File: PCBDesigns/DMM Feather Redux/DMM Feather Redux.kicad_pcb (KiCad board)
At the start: 4 copper layers, 116.2 x 93.3 mm, 49 parts, among them J10 I_Input, J14 Barrel_Jack, J2 Conn_01x03_Pin, J3 Conn_01x04_MountingPin, J7 Barrel_Jack, Q2 AO3400A MOSFET, Q8 AO3400A MOSFET, SW3 SW_SPDT, U10 LM4040DBZ-2.5, U13 ISO1540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

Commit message: Work on different PCBs. Mostly.
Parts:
- removed A1: Adafruit_Feather_32u4_BluefruitLE, Module:Adafruit_Feather_WithMountingHoles
- removed H1, H2, H3: MountingHole, MountingHole:MountingHole_2.2mm_M2_Pad
- removed H4: MountingHole, MountingHole:MountingHole_2.2mm_M2_ISO14580
- removed J2: Conn_01x03_Pin, Connector_PinHeader_2.54mm:PinHeader_1x03_P2.54mm_Vertical
- removed R6, R7: 4.7K, Resistor_SMD:R_0805_2012Metric_Pad1.20x1.40mm_HandSolder
- added A2: Adafruit_Feather_32u4_BluefruitLE, Module:Adafruit_Feather_WithMountingHoles, F.Cu at (47.9, 64.3)
- added D1: LED, LED_SMD:LED_Luminus_MP-3030-1100_3.0x3.0mm, F.Cu at (143.5, 80.2)
- added J5: Conn_01x12_Pin, Connector_PinSocket_2.54mm:PinSocket_1x12_P2.54mm_Vertical, F.Cu at (126.2, 93.2)
- added J6: Conn_01x16_Pin, Connector_PinSocket_2.54mm:PinSocket_1x16_P2.54mm_Vertical, F.Cu at (116.1, 113.5)
- added J9: Out to Screen, Connector_PinSocket_2.54mm:PinSocket_1x04_P2.54mm_Vertical, F.Cu at (221.4, 71.1)
- added Q1: MMBT3904, Package_TO_SOT_SMD:SOT-23, F.Cu at (148.3, 80.2)
- added R4: 500, Resistor_SMD:R_0805_2012Metric_Pad1.20x1.40mm_HandSolder, F.Cu at (154.9, 80.2)
- added RN1: R_Pack04_Split, Resistor_SMD:R_Array_Convex_4x0603, F.Cu at (158.1, 98.0)
- added SW1: SW_Push, Button_Switch_SMD:SW_SPST_CK_RS282G05A3, F.Cu at (131.3, 76.6)
- added SW2: SW_Push, Button_Switch_SMD:SW_SPST_CK_RS282G05A3, F.Cu at (131.3, 81.8)
- added SW4: SW_Push, Button_Switch_SMD:SW_SPST_CK_RS282G05A3, F.Cu at (131.3, 86.9)
- C17, C4, C7, C8: footprint Capacitor_SMD:C_0805_2012Metric_Pad1.18x1.45mm_HandSolder -> Capacitor_SMD:C_0603_1608Metric
- R1, R10, R11, R12, R19, R2, R27: footprint Resistor_SMD:R_0805_2012Metric_Pad1.20x1.40mm_HandSolder -> Resistor_SMD:R_0603_1608Metric
- R5: value 4.7K -> 1K; footprint Resistor_SMD:R_0805_2012Metric_Pad1.20x1.40mm_HandSolder -> Resistor_SMD:R_0603_1608Metric
- moved U4 60.5 mm to (135.9, 103.3), turned to 90 degrees
- moved J7 52.0 mm to (183.4, 89.9), turned to 180 degrees
- moved J3 33.6 mm to (117.2, 93.7)
- moved C7 32.0 mm to (145.5, 108.0), turned to 180 degrees
- moved R10 32.0 mm to (175.4, 114.4), turned to 180 degrees
- moved C6 31.2 mm to (165.5, 82.0), turned to 90 degrees
- moved J10 30.0 mm to (187.5, 74.0)
- moved U6 30.0 mm to (168.6, 82.0), turned to 90 degrees
- moved R2 28.9 mm to (151.2, 98.4), turned to 180 degrees
- moved R12 28.4 mm to (157.7, 108.8)
- moved Q8 27.8 mm to (171.8, 111.8), turned to 90 degrees
- moved J14 26.7 mm to (183.5, 106.2), turned to 180 degrees
- moved R17 25.6 mm to (176.9, 109.3), turned to 180 degrees
- moved U13 25.3 mm to (145.4, 103.1), turned to -90 degrees
- moved SW3 24.6 mm to (118.8, 78.6), turned to -90 degrees
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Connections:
- net /MOSFET_Gate renamed /V_Bridge_Ctrl-ISO
- R5 pad 1: 5V-iso -> /LED_Ctrl_ISO
- R5 pad 2: SCL-5V -> Net-(Q1-B)
- U4 pad 11: unconnected-(U4-VOD-Pad11) -> /LED_Ctrl_ISO
- U4 pad 6: unconnected-(U4-VID-Pad6) -> /LED_Ctrl
- U5 pad 3: /Driver_U2_Out_B -> /I_Supply_Ohmmeter
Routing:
- net SCL: track 48.3 -> 0.00 mm, vias 1 -> 0
- net SDA: track 44.6 -> 0.00 mm, vias 3 -> 0
- net /R Circuit I Output: track 0.00 -> 25.7 mm
- net VDD: track 21.9 -> 0.00 mm, vias 1 -> 0
- net SDA-5V: track 24.5 -> 3.34 mm, vias 2 -> 0
- net 5V-iso: track 22.0 -> 3.75 mm, vias 7 -> 2
- net /V_Bridge_Ctrl-ISO: track 31.9 -> 14.6 mm
- net Net-(Q2-S): track 0.00 -> 17.2 mm
- net SCL-5V: track 20.2 -> 3.38 mm, vias 2 -> 0
- net GND: track 15.2 -> 0.00 mm
- net Net-(Q2-G): track 0.00 -> 15.0 mm, vias 0 -> 2
- net Gnd-iso: track 28.0 -> 15.9 mm, vias 6 -> 8
- net ADS_ALERT: track 11.8 -> 0.00 mm
- net Net-(U5-VO): track 0.00 -> 9.45 mm
- net ADS_ADDR: track 8.07 -> 0.00 mm
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- removed copper zone on In1.Cu, net GND
- removed copper zone on In2.Cu, net VDD
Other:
- board size 116.2 x 93.3 mm -> 80.9 x 47.9 mm

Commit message: More PCB work.
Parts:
- moved A2 84.1 mm to (116.1, 113.5)
- moved J9 41.2 mm to (180.2, 72.4)
- moved R19 14.5 mm to (168.5, 94.2)
- moved SW1 10.2 mm to (131.3, 86.9)
- moved SW4 9.21 mm to (131.3, 77.7)
- moved R4 6.99 mm to (148.0, 80.0)
- moved J3 6.53 mm to (119.5, 87.6)
- moved R12 6.41 mm to (164.1, 108.8)
- moved C4 6.33 mm to (161.2, 103.6)
- moved U3 6.33 mm to (164.3, 103.6)
- moved U10 6.21 mm to (169.4, 101.2)
- moved J10 4.85 mm to (192.3, 74.9)
- moved Q1 4.78 mm to (148.0, 75.5)
- moved D1 4.56 mm to (143.9, 75.6), turned to 90 degrees
- moved SW3 4.06 mm to (120.2, 74.8)
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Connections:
- net Net-(A2-EN) renamed EN
- A2 pad 10: unconnected-(A2-A5-Pad10) -> A5
- A2 pad 11: unconnected-(A2-SCK/D15-Pad11) -> SCK
- A2 pad 12: unconnected-(A2-MOSI/D16-Pad12) -> MOSI
- A2 pad 13: unconnected-(A2-MISO/D14-Pad13) -> MISO
- A2 pad 14: unconnected-(A2-RX/D0-Pad14) -> RX
- A2 pad 15: unconnected-(A2-TX/D1-Pad15) -> TX
- A2 pad 19: /V_Bridge_Ctrl-MCU -> D5
- A2 pad 20: /LED_Ctrl -> D6
- A2 pad 21: /D9_(OhmmeterBridge_ctrl) -> D9
- A2 pad 22: /D10_(Ohmmeter_I_ctrl) -> D10
- A2 pad 26: unconnected-(A2-USB-Pad26) -> USB
- A2 pad 28: unconnected-(A2-VBAT-Pad28) -> VBAT
- A2 pad 5: unconnected-(A2-A0-Pad5) -> A0
- A2 pad 6: unconnected-(A2-A1-Pad6) -> A1
- A2 pad 7: unconnected-(A2-A2-Pad7) -> A2
- A2 pad 8: unconnected-(A2-A3-Pad8) -> A3
- A2 pad 9: unconnected-(A2-A4-Pad9) -> A4
- D1 pad 1: GND -> Gnd-iso
- J5 pad 1: unconnected-(J5-Pin_1-Pad1) -> VBAT
- J5 pad 10: /V_Bridge_Ctrl-MCU -> D5
- J5 pad 3: unconnected-(J5-Pin_3-Pad3) -> USB
- J5 pad 4: unconnected-(J5-Pin_4-Pad4) -> D13
- J5 pad 5: unconnected-(J5-Pin_5-Pad5) -> D12
- J5 pad 6: unconnected-(J5-Pin_6-Pad6) -> D11
- J5 pad 7: /D10_(Ohmmeter_I_ctrl) -> D10
- J5 pad 8: /D9_(OhmmeterBridge_ctrl) -> D9
- J5 pad 9: unconnected-(J5-Pin_9-Pad9) -> D6
- J6 pad 1: unconnected-(J6-Pin_1-Pad1) -> RESET
- J6 pad 10: unconnected-(J6-Pin_10-Pad10) -> A5
- J6 pad 11: unconnected-(J6-Pin_11-Pad11) -> SCK
- J6 pad 12: unconnected-(J6-Pin_12-Pad12) -> MOSI
- J6 pad 13: unconnected-(J6-Pin_13-Pad13) -> MISO
- J6 pad 14: unconnected-(J6-Pin_14-Pad14) -> RX
- J6 pad 15: unconnected-(J6-Pin_15-Pad15) -> TX
- J6 pad 3: unconnected-(J6-Pin_3-Pad3) -> VDD
- J6 pad 5: unconnected-(J6-Pin_5-Pad5) -> A0
- J6 pad 6: unconnected-(J6-Pin_6-Pad6) -> A1
- J6 pad 7: unconnected-(J6-Pin_7-Pad7) -> A2
- J6 pad 8: unconnected-(J6-Pin_8-Pad8) -> A3
- J6 pad 9: unconnected-(J6-Pin_9-Pad9) -> A4
- J9 pad 1: SDA-5V -> SDA
- J9 pad 2: SCL-5V -> SCL
- RN1 pad 2: unconnected-(RN1B-R2.1-Pad2) -> 5V-iso
- U4 pad 3: /D9_(OhmmeterBridge_ctrl) -> D5
- U4 pad 4: /D10_(Ohmmeter_I_ctrl) -> D6
- U4 pad 5: /V_Bridge_Ctrl-MCU -> D9
- U4 pad 6: /LED_Ctrl -> D10
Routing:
- net /AIN3: track 0.00 -> 36.2 mm, vias 0 -> 2
- net Gnd-iso: track 15.9 -> 49.6 mm, vias 8 -> 14
- net D11: track 0.00 -> 20.3 mm
- net D5: track 0.00 -> 16.1 mm
- net SDA-5V: track 3.34 -> 18.7 mm
- net SCL-5V: track 3.38 -> 18.7 mm, vias 0 -> 2
- net D6: track 0.00 -> 15.0 mm
- net D12: track 0.00 -> 14.8 mm
- net D9: track 0.00 -> 13.7 mm
- net Net-(Q2-S): track 17.2 -> 30.0 mm
- net SDA: track 0.00 -> 12.7 mm, vias 0 -> 2
- net D10: track 0.00 -> 12.5 mm
- net SCL: track 0.00 -> 11.9 mm, vias 0 -> 2
- net 5V-iso: track 3.75 -> 15.5 mm, vias 2 -> 6
- net ADS_ALERT: track 0.00 -> 11.2 mm, vias 0 -> 2
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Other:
- board size 80.9 x 47.9 mm -> 83.4 x 47.9 mm

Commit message: PCB Work.
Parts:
- removed A2: Adafruit_Feather_32u4_BluefruitLE, Module:Adafruit_Feather_WithMountingHoles
- removed J3: Conn_01x04_MountingPin, Connector_JST:JST_SH_SM04B-SRSS-TB_1x04-1MP_P1.00mm_Horizontal
- removed SW3: SW_SPDT, Button_Switch_THT:SW_Slide_SPDT_Angled_CK_OS102011MA1Q
- added C10: 0.1uF, Capacitor_SMD:C_0603_1608Metric, F.Cu at (140.6, 97.8)
- added C11: 0.1uF, Capacitor_SMD:C_0603_1608Metric, F.Cu at (137.9, 110.5)
- added SW5: MS-22D28-G020, Library:SW-SMD_MS-22D28-G020, F.Cu at (119.4, 81.9)
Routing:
- net GND: track 3.09 -> 52.7 mm, vias 0 -> 7
- net Gnd-iso: track 49.6 -> 96.3 mm, vias 14 -> 17
- net VDD: track 3.18 -> 45.1 mm, vias 0 -> 3
- net /V_Bridge_Ctrl-ISO: track 5.41 -> 46.2 mm, vias 0 -> 2
- net 5V-iso: track 15.5 -> 54.7 mm, vias 6 -> 7
- net /LED_Ctrl_ISO: track 0.00 -> 36.9 mm, vias 0 -> 2
- net /OhmmeterBridgeCtrl_ISO: track 0.00 -> 36.4 mm, vias 0 -> 2
- net /Ohmmeter_I_ctrl_ISO: track 0.00 -> 35.3 mm, vias 0 -> 2
- net SDA: track 12.7 -> 47.4 mm
- net SCL: track 11.9 -> 46.6 mm
- net EN: track 0.00 -> 17.4 mm
- net Net-(J10-Pin_2): track 2.99 -> 8.14 mm
- net ADS_ALERT: track 11.2 -> 14.8 mm
- net SDA-5V: track 18.7 -> 22.3 mm, vias 0 -> 2
- net SCL-5V: track 18.7 -> 22.0 mm
- added copper zone on In1.Cu, net GND
- added copper zone on In2.Cu, net VDD
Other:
- board size 83.4 x 47.9 mm -> 85.5 x 47.4 mm

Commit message: PCB Work
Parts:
- SW1, SW2, SW4: footprint Button_Switch_SMD:SW_SPST_CK_RS282G05A3 -> Button_Switch_SMD:SW_Push_1P1T-SH_NO_CK_KMR2xxG
- moved SW2 40.0 mm to (94.9, 98.7)
- moved SW4 34.4 mm to (100.1, 92.3)
- moved SW1 31.4 mm to (104.3, 102.7)
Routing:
- net Gnd-iso: track 96.3 -> 92.8 mm, vias 17 -> 16
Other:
- board text added: "OIH Designs Feather-Based DMM 20260529"
- board text removed: "OIH Designs | Voltmeter Above Ground Bias w Open Lead Detect Vout = (+Vin/((R17+18)/R24))-VRef) Input safe voltages only w/o extra precautions & testing."

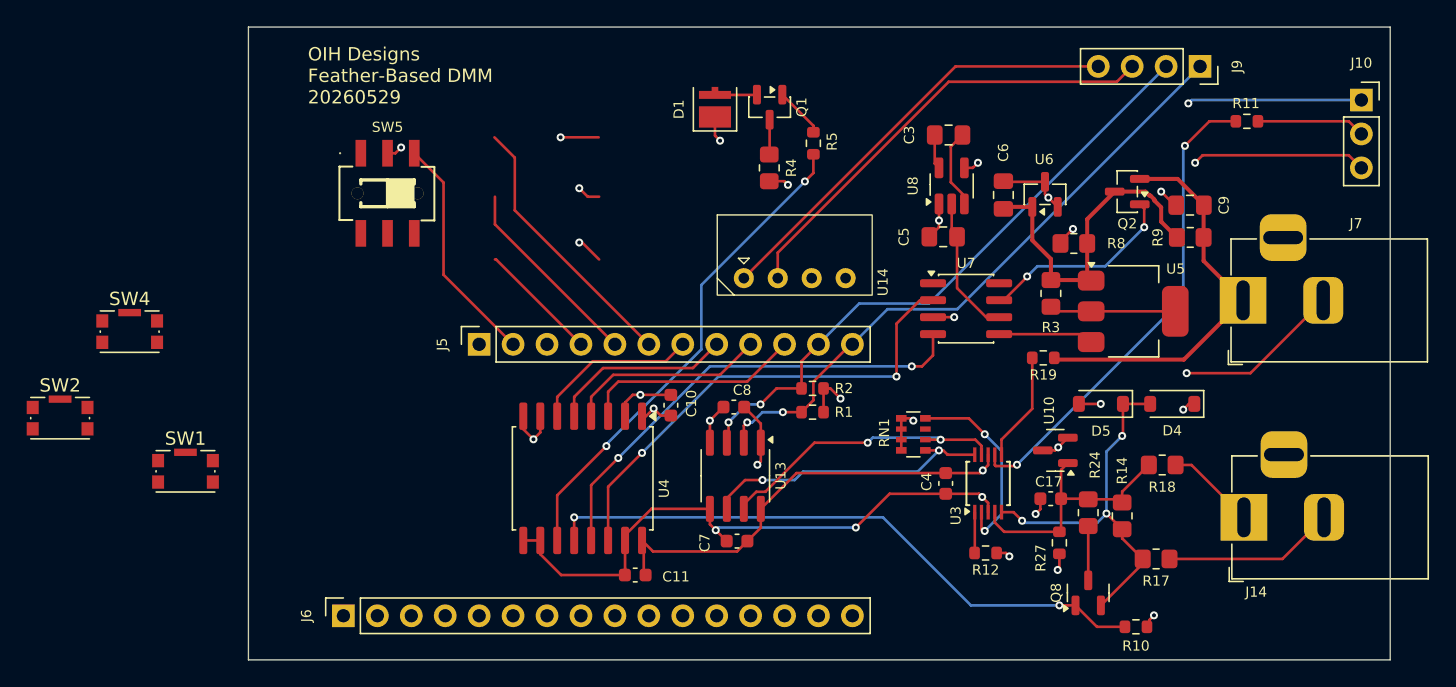
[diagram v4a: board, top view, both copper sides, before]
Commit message: DMM PCB work and Voltmeter Sketch Updates
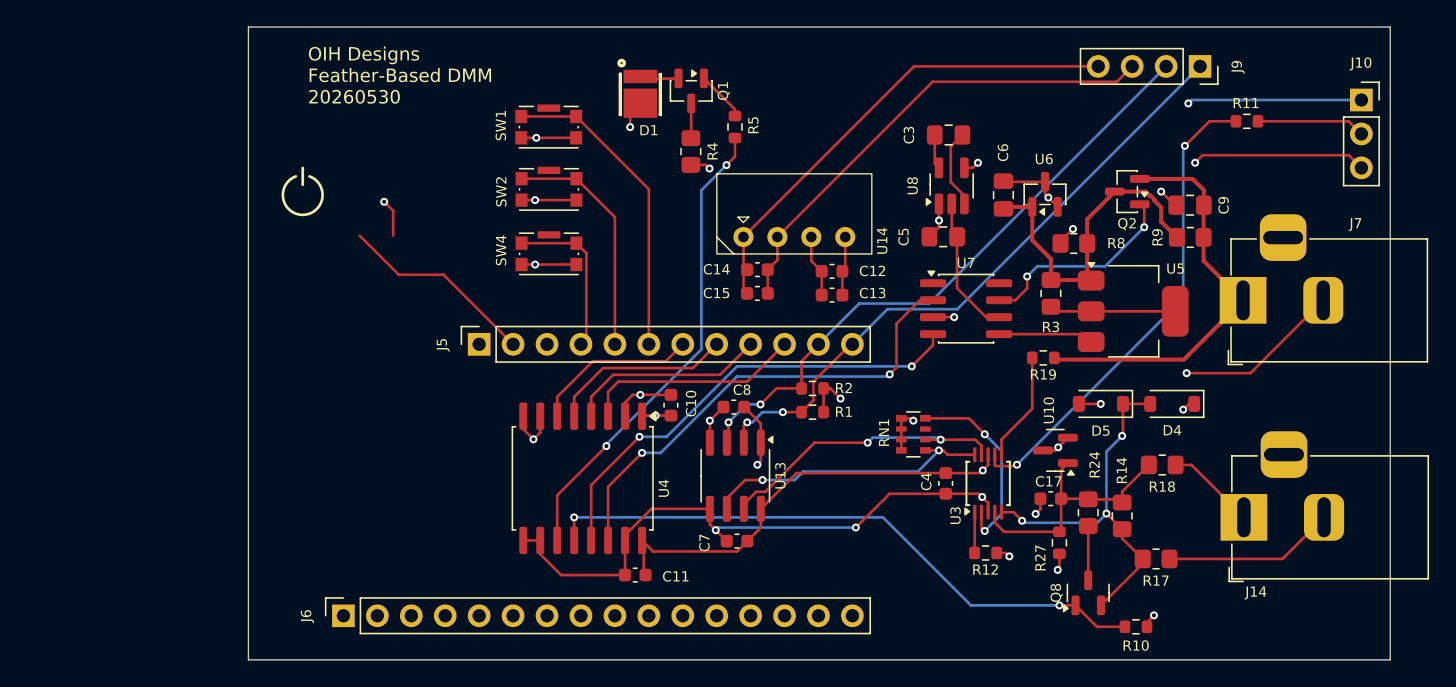
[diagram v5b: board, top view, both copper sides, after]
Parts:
- removed SW5: MS-22D28-G020, Library:SW-SMD_MS-22D28-G020
- added C12: 10uF, Capacitor_SMD:C_0603_1608Metric, F.Cu at (152.7, 87.8)
- added C13: 0.1uF, Capacitor_SMD:C_0603_1608Metric, F.Cu at (152.7, 89.5)
- added C14: 10uF, Capacitor_SMD:C_0603_1608Metric, F.Cu at (147.1, 87.6)
- added C15: 0.1uF, Capacitor_SMD:C_0603_1608Metric, F.Cu at (147.1, 89.4)
- D1: footprint LED_SMD:LED_Luminus_MP-3030-1100_3.0x3.0mm -> Custom:LED-SMD_L3.0-W3.0_WHITE
- moved SW2 40.4 mm to (131.5, 81.6)
- moved SW1 37.5 mm to (131.4, 77.0)
- moved SW4 31.9 mm to (131.5, 86.4)
- moved Q1 5.99 mm to (142.1, 74.2)
- moved R4 5.99 mm to (142.1, 78.8)
- moved R5 5.99 mm to (145.4, 76.9)
- moved D1 5.77 mm to (138.3, 74.2), turned to -90 degrees
- moved U14 3.08 mm to (151.1, 84.1)
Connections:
- D1 pad 1: Gnd-iso -> Net-(D1-A)
- D1 pad 2: Net-(D1-A) -> Gnd-iso
- SW1 pad 1: D13 -> D11
- SW4 pad 1: D11 -> D13
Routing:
- net GND: track 52.7 -> 63.1 mm
- net 5V-iso: track 54.7 -> 59.1 mm
- net Gnd-iso: track 92.8 -> 96.6 mm
- net D11: track 20.3 -> 23.4 mm
- net D13: track 9.07 -> 12.1 mm
- net D12: track 14.8 -> 17.7 mm
- net EN: track 17.4 -> 14.8 mm
- net VDD: track 45.1 -> 46.9 mm
- net /LED_Ctrl_ISO: track 36.9 -> 35.6 mm
- net Net-(Q2-S): track 30.0 -> 30.6 mm
- net Net-(Q2-G): track 15.0 -> 15.5 mm
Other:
- board text added: "OIH Designs Feather-Based DMM 20260530"
- board text removed: "OIH Designs Feather-Based DMM 20260529"

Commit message: Circuits, mostly
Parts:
- added A2: Adafruit_Feather_32u4_BluefruitLE, Module:Adafruit_Feather_WithMountingHoles, F.Cu at (1.76, 6.62)
- added J1: Conn_01x02, Connector_PinSocket_2.54mm:PinSocket_1x02_P2.54mm_Vertical, F.Cu at (116.7, 83.3)
- added J2: Conn_01x02, Connector_PinSocket_2.54mm:PinSocket_1x02_P2.54mm_Vertical, F.Cu at (124.3, 102.1)
- added R20: 240k, Resistor_SMD:R_0805_2012Metric, F.Cu at (179.2, 103.4)
- added R21: 240k, Resistor_SMD:R_0805_2012Metric, F.Cu at (178.0, 111.8)
- R14, R24, R3, R4, R8, R9: footprint Resistor_SMD:R_0805_2012Metric_Pad1.20x1.40mm_HandSolder -> Resistor_SMD:R_0805_2012Metric
- R17, R18: value 499.0K -> 240k; footprint Resistor_SMD:R_0805_2012Metric_Pad1.20x1.40mm_HandSolder -> Resistor_SMD:R_0805_2012Metric
- moved D5 19.0 mm to (160.4, 112.1)
- moved D4 19.0 mm to (165.7, 112.1)
- moved R10 17.9 mm to (159.5, 106.2)
- moved R18 2.24 mm to (175.1, 102.2)
- moved R17 0.76 mm to (176.1, 109.3)
- moved SW1 0.25 mm to (131.4, 76.7)
- renumbered SW4 to SW3
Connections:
- R17 pad 1: V_Input_Float -> Net-(R17-Pad1)
- R18 pad 1: V_Input_REF -> Net-(R18-Pad1)
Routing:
- net VBAT: track 0.00 -> 9.68 mm
- net Net-(R18-Pad1): track 0.00 -> 3.25 mm
- net GND: track 63.1 -> 60.3 mm, vias 7 -> 6
- net /V_Bridge_Ctrl-ISO: track 46.2 -> 43.6 mm, vias 2 -> 3
- net Net-(R17-Pad1): track 0.00 -> 2.44 mm
- net /AIN1: track 28.5 -> 26.3 mm
- net 5V-iso: track 59.1 -> 61.1 mm, vias 7 -> 6
- net V_Input_REF: track 6.74 -> 5.07 mm
- net Gnd-iso: track 96.6 -> 98.0 mm, vias 16 -> 15
- net EN: track 14.8 -> 16.2 mm
- net /LED_Ctrl_ISO: track 35.6 -> 36.3 mm
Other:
- outline, holes or cut-outs redrawn
- board text added: "+"
- board text added: "Battery"

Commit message: More Giga Logger Updates
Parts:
- added A1: Arduino_UNO_R3, Module:Arduino_UNO_R3, B.Cu at (59.8, 115.8)
- moved R11 4.13 mm to (187.8, 76.7)
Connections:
- J10 pad 1: 5V-iso -> VDD
- J10 pad 3: Gnd-iso -> GND
- R11 pad 1: /AIN3 -> A0
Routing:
- net A0: track 0.00 -> 77.0 mm, vias 0 -> 1
- net /AIN3: track 36.2 -> 0.00 mm, vias 2 -> 0
- net GND: track 60.3 -> 83.1 mm, vias 6 -> 7
- net VDD: track 46.9 -> 65.1 mm
- net Gnd-iso: track 98.0 -> 84.9 mm, vias 15 -> 14
- net 5V-iso: track 61.1 -> 48.1 mm, vias 6 -> 5
- net Net-(J10-Pin_2): track 8.14 -> 3.94 mm
- net /AIN1: track 26.3 -> 25.7 mm
